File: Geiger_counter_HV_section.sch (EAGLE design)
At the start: 20 parts, among them IC1 TLC555, Q1 MMBT3904, Q2 KSC5502

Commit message: Updated
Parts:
- R1: value 330 -> 10k
- R2: value 1k -> 330
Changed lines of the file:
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@@
 <part name="D1" library="thomas_library" deviceset="DIODE" device="0805" value="1N914"/>
 <part name="C1" library="thomas_library" deviceset="CAPACITOR" device="0805" value="1nF"/>
-<part name="R1" library="thomas_library" deviceset="RESISTOR" device="0805" technology="SMD" value="330"/>
-<part name="R2" library="thomas_library" deviceset="RESISTOR" device="0805" technology="SMD" value="1k"/>
+<part name="R1" library="thomas_library" deviceset="RESISTOR" device="0805" technology="SMD" value="10k"/>
+<part name="R2" library="thomas_library" deviceset="RESISTOR" device="0805" technology="SMD" value="330"/>
 <part name="R3" library="thomas_library" deviceset="RESISTOR" device="0805" technology="SMD" value="220k"/>
 <part name="R4" library="thomas_library" deviceset="RESISTOR" device="0805" technology="SMD" value="100k"/>

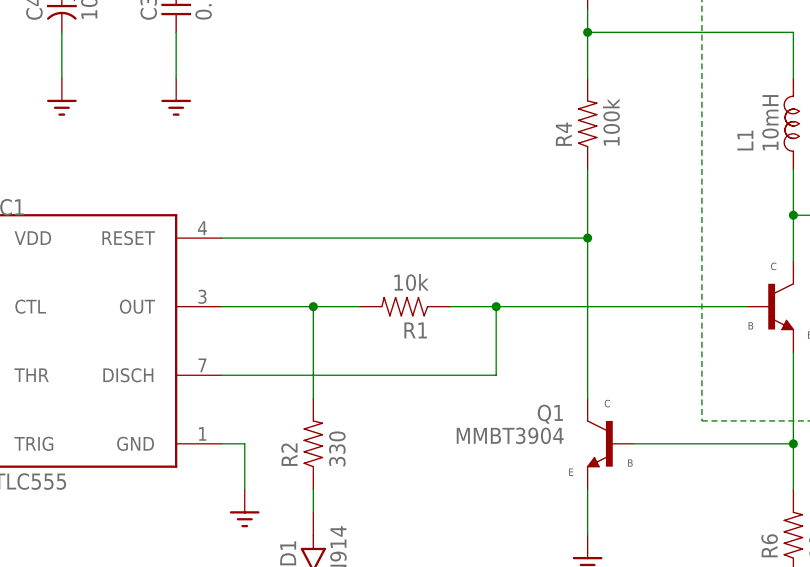
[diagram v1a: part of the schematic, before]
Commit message: Part value modification
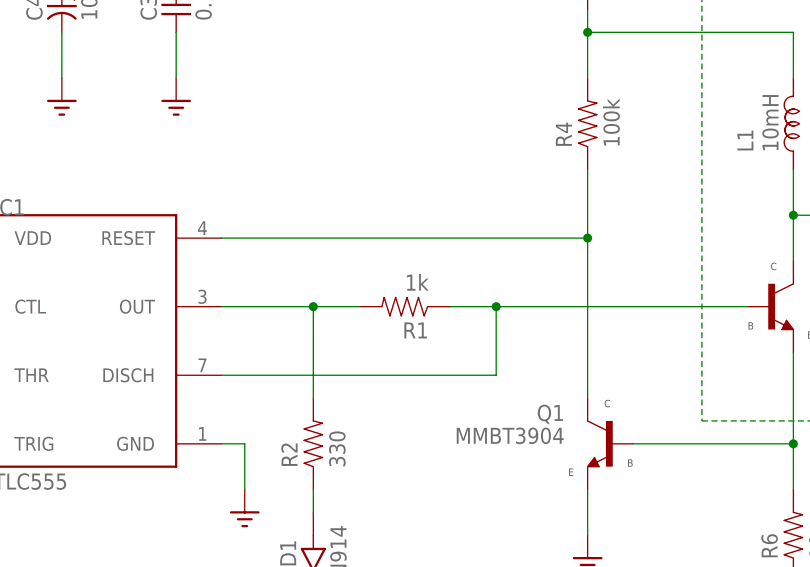
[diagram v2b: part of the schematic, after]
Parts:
- R1: value 10k -> 1k
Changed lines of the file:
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@@
 <part name="D1" library="thomas_library" deviceset="DIODE" device="0805" value="1N914"/>
 <part name="C1" library="thomas_library" deviceset="CAPACITOR" device="0805" value="1nF"/>
-<part name="R1" library="thomas_library" deviceset="RESISTOR" device="0805" technology="SMD" value="10k"/>
+<part name="R1" library="thomas_library" deviceset="RESISTOR" device="0805" technology="SMD" value="1k"/>
 <part name="R2" library="thomas_library" deviceset="RESISTOR" device="0805" technology="SMD" value="330"/>
 <part name="R3" library="thomas_library" deviceset="RESISTOR" device="0805" technology="SMD" value="220k"/>
